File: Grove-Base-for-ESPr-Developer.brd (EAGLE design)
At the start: 26 x 26 mm, 8 parts, among them J1 4P-2.0, J2 4P-2.0, J3 4P-2.0, J4 4P-2.0

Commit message: 1st 5V evt
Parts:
- added R10, R11, R12, R13, R14, R3, R4, R5, R6, R7, R8, R9: 1K, Seeed-OPL-Resistor:R0603
- added R15: 27K, Seeed-OPL-Resistor:R0603
- added T1, T2, T3, T4, T5, T6: (no value), we-transistor:SOT23
- R1: value 220K -> 200K
- R2: value 100K -> 24K
- moved R1 7.18 mm to (20.3, 17.8), turned to 270 degrees
- moved R2 3.42 mm to (20.3, 15.9), turned to 90 degrees
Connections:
- new net IO12_5V: J2.1, R8.1, T3.3
- new net IO13_5V: J2.2, R10.2, T4.3
- new net IO14_5V: J1.1, R4.2, T1.3
- new net IO15_5V: J1.2, R6.2, T2.3
- new net IO4_5V: J4.2, R14.2, T6.3
- new net IO5_5V: J4.1, R12.1, T5.3
- new net N$6: R15.2, R2.1
- net 3V3: now also R11.2, R13.1, R3.1, R5.1, R7.2, R9.1, T1.1, T2.1, T3.1, T4.1, T5.1, T6.1; no longer J1.3, J2.3, J3.3, J4.3
- net 5V: now also J1.3, J2.3, J3.3, J4.3, R10.1, R12.2, R14.1, R4.1, R6.1, R8.2
- net GND: now also R15.1; no longer R2.1
- net IO12: now also R7.1, T3.2; no longer J2.1
- net IO13: now also R9.2, T4.2; no longer J2.2
- net IO14: now also R3.2, T1.2; no longer J1.1
- net IO15: now also R5.2, T2.2; no longer J1.2
- net IO4: now also R13.2, T6.2; no longer J4.2
- net IO5: now also R11.1, T5.2; no longer J4.1
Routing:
- net 5V: track 0.00 -> 82.9 mm, vias 0 -> 1
- net IO14_5V: track 0.00 -> 30.0 mm
- net 3V3: track 41.6 -> 70.8 mm, vias 1 -> 3
- net IO5_5V: track 0.00 -> 18.3 mm, vias 0 -> 2
- net IO14: track 24.2 -> 6.97 mm
- net IO15_5V: track 0.00 -> 15.3 mm
- net IO4_5V: track 0.00 -> 10.0 mm
- net IO12_5V: track 0.00 -> 9.71 mm
- net IO15: track 19.8 -> 10.2 mm
- net IO13_5V: track 0.00 -> 8.22 mm
- net A0: track 13.0 -> 5.48 mm
- net IO4: track 21.6 -> 15.3 mm, vias 0 -> 1
- net GND: track 68.2 -> 74.3 mm, vias 1 -> 0
- net IO5: track 19.2 -> 13.6 mm, vias 0 -> 1
- net IO12: track 11.7 -> 7.03 mm
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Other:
- board text added: "CC: BY-SA K. Hino Sep 29 2016"
- board text removed: "CC: BY-SA S. Kobayashi June 20 2016"

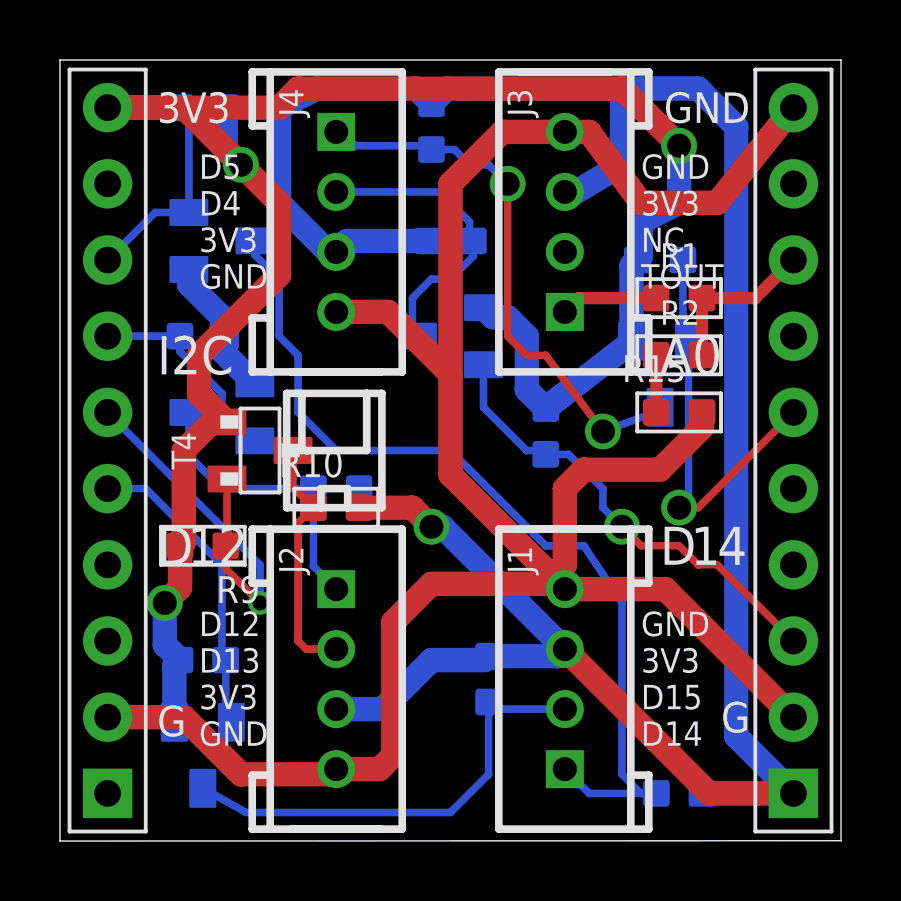
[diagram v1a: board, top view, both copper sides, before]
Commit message: 2nd EVT
2nd EVT (for hand soldering...)
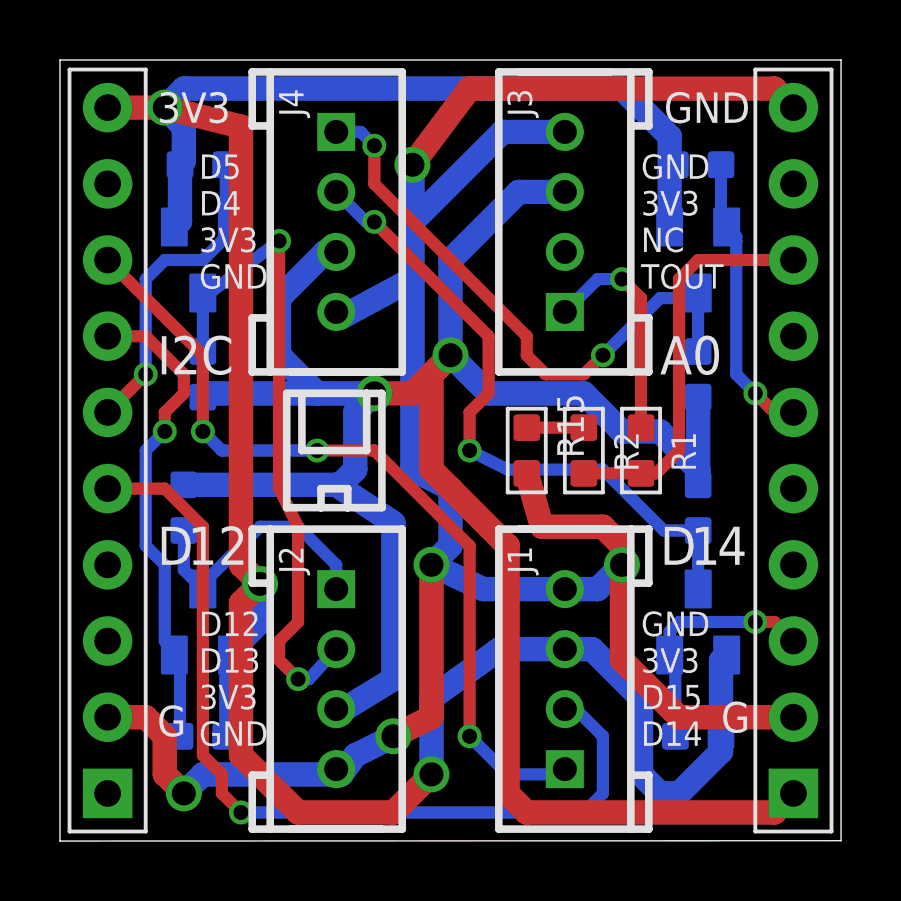
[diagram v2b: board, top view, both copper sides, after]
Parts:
- removed R3, R4, R5, R6: 1K, Seeed-OPL-Resistor:R0603
- removed T1, T2: (no value), we-transistor:SOT23
- R10, R11, R12, R13, R14, R7, R8, R9: value 1K -> 10K
- moved R7 13.3 mm to (4.45, 3.17)
- moved R9 12.7 mm to (4.45, 22.2), flipped to the bottom, turned to 270 degrees
- moved T6 12.6 mm to (21.0, 6.99), turned to 90 degrees
- moved R12 12.1 mm to (21.0, 15.2), turned to 0 degrees
- moved R14 12.1 mm to (21.0, 10.8), turned to 0 degrees
- moved R13 11.4 mm to (21.0, 3.17), turned to 90 degrees
- moved T3 7.01 mm to (4.45, 6.99), turned to 90 degrees
- moved T4 6.63 mm to (4.45, 19.1), flipped to the bottom, turned to 270 degrees
- moved R10 6.29 mm to (4.45, 15.2), flipped to the bottom, turned to 180 degrees
- moved R1 5.24 mm to (19.1, 12.7), turned to 180 degrees
- moved R15 5.24 mm to (15.2, 12.7), turned to 180 degrees
- moved R8 5.12 mm to (3.81, 10.8), turned to 180 degrees
- moved R2 4.49 mm to (17.1, 12.7), turned to 0 degrees
- moved T5 4.02 mm to (21.0, 19.1)
- moved R11 3.42 mm to (21.0, 22.2)
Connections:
- removed net IO14_5V: J1.1, R4.2, T1.3
- removed net IO15_5V: J1.2, R6.2, T2.3
- net 3V3: now also J1.3; no longer R3.1, R5.1, T1.1, T2.1
- net 5V: no longer J1.3, R4.1, R6.1
- net IO14: now also J1.1; no longer R3.2, T1.2
- net IO15: now also J1.2; no longer R5.2, T2.2
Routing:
- net IO14_5V: track 30.0 -> 0.00 mm
- net IO14: track 6.97 -> 27.6 mm, vias 0 -> 3
- net IO15: track 10.2 -> 29.6 mm, vias 0 -> 1
- net IO15_5V: track 15.3 -> 0.00 mm
- net 3V3: track 70.8 -> 84.7 mm
- net IO13_5V: track 8.22 -> 22.1 mm, vias 0 -> 2
- net IO4_5V: track 10.0 -> 21.7 mm, vias 0 -> 2
- net IO12: track 7.03 -> 16.1 mm, vias 0 -> 1
- net A0: track 5.48 -> 13.3 mm
- net IO4: track 15.3 -> 8.09 mm
- net N$5: track 3.24 -> 7.57 mm, vias 0 -> 1
- net GND: track 74.3 -> 78.5 mm, vias 0 -> 5
- net IO5: track 13.6 -> 10.2 mm
- net IO13: track 13.7 -> 10.8 mm
- net 5V: track 82.9 -> 80.6 mm, vias 1 -> 2
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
